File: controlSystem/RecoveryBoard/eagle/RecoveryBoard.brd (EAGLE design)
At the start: 120.9 x 54.6 mm, 104 parts, among them Q1 BSS123, Q2 BSS123, Q3 BSS123, Q4 BPR-301, Q5 BPR-301, Q6 MOSFET-PCH-SOT23-6, Q7 SI7465DP-T1-E3, U1 STM32F042K6, U10 TPS63070, U2 BD62120AEFJ-E2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

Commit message: updating firmware doc
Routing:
- net GND: vias 187 -> 186

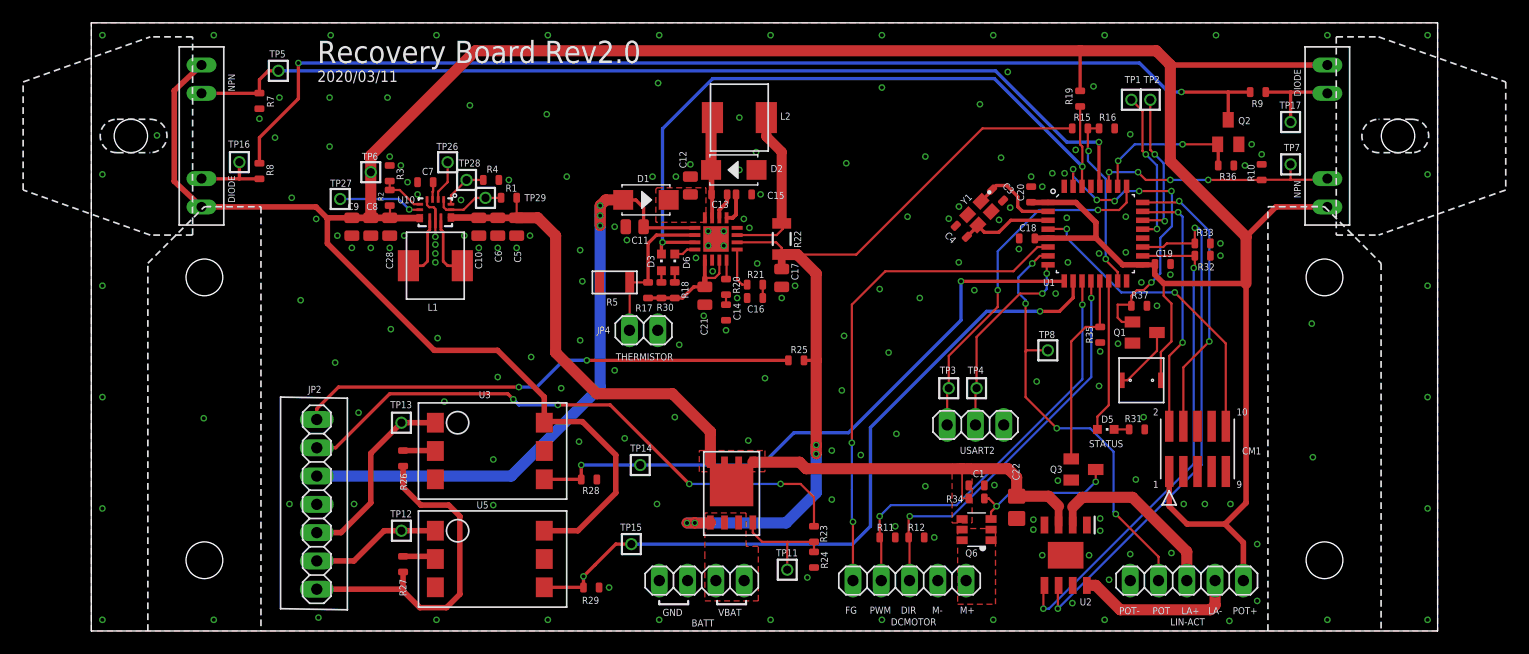
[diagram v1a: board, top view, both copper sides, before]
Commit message: added fastener restrictions and more satisfying via placement
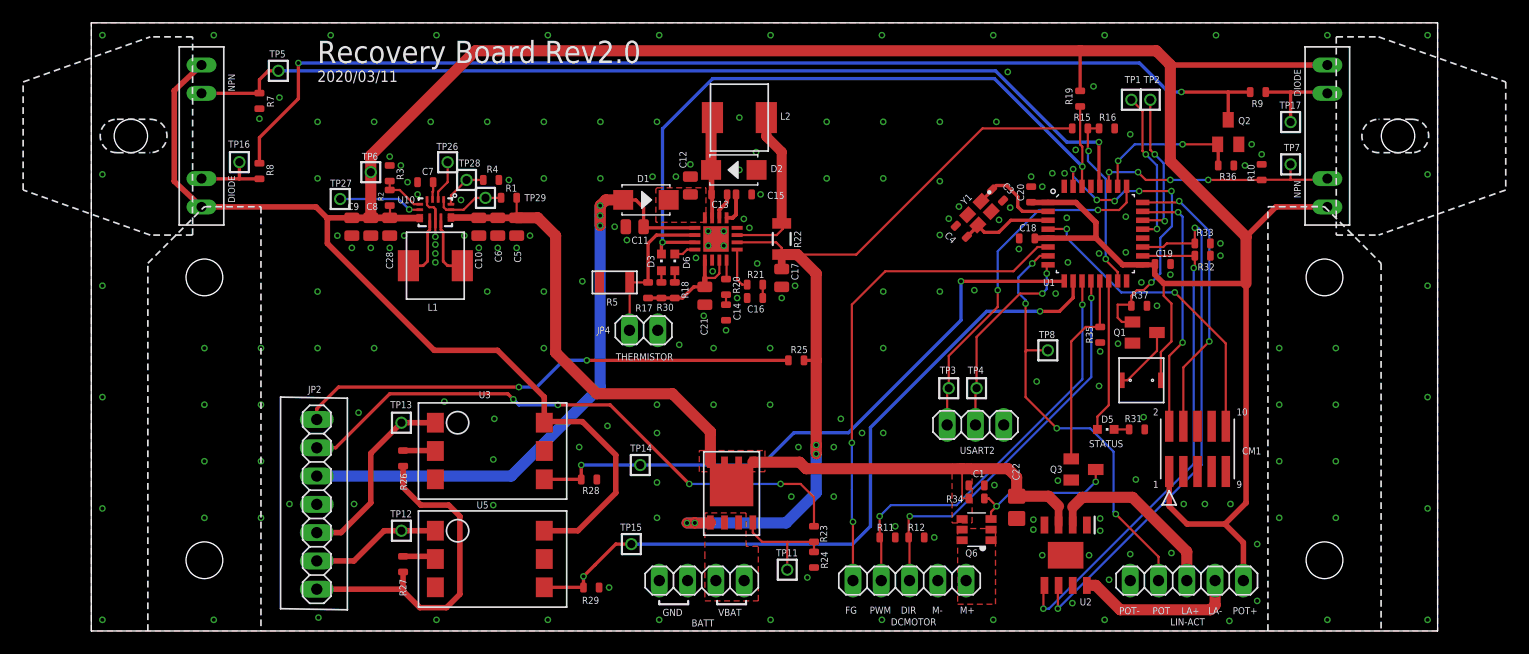
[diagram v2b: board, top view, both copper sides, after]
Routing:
- net GND: vias 186 -> 200
